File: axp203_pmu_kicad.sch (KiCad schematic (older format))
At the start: 0 parts

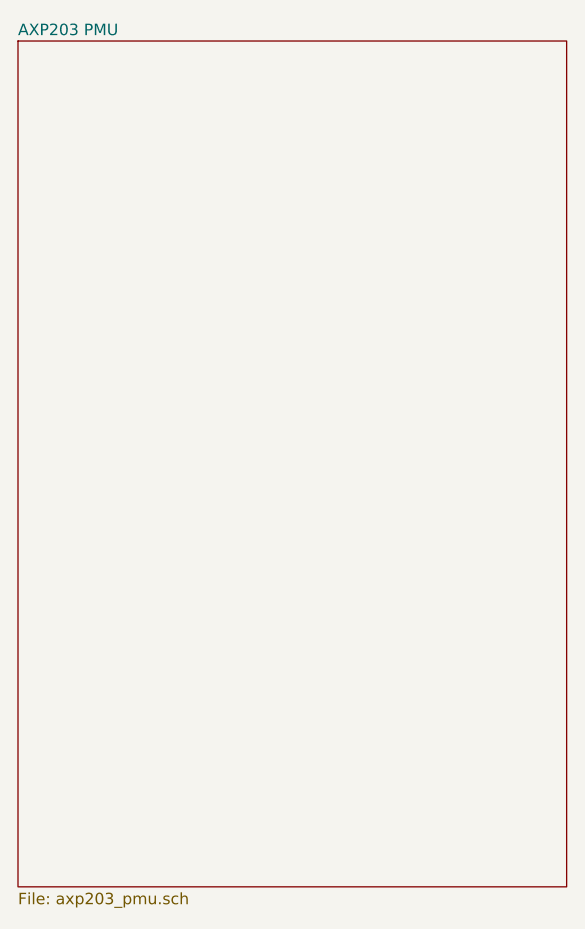
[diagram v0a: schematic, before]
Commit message: Schematic finished, pcb components added in pcb, axp schematic checked
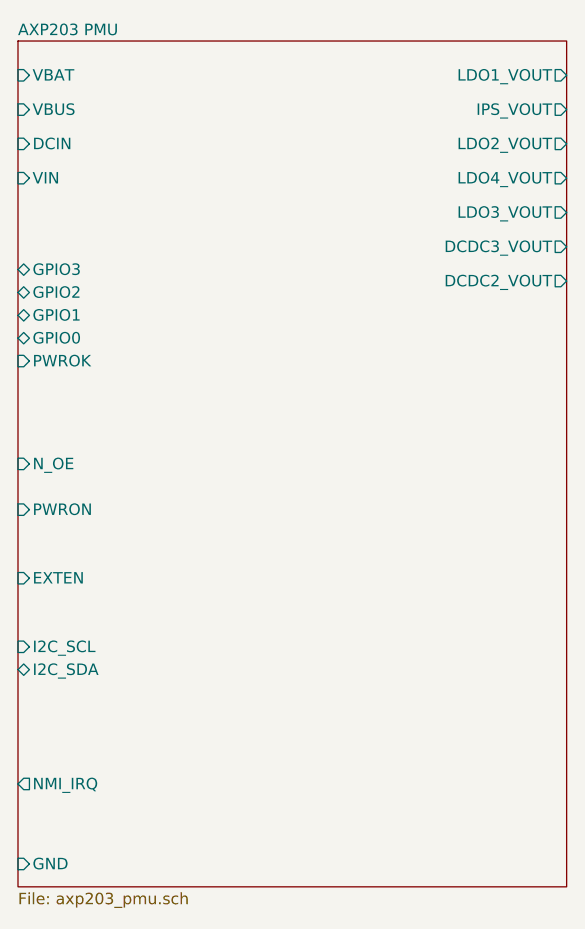
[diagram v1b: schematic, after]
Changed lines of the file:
@@
 F0 "AXP203 PMU" 50
 F1 "axp203_pmu.sch" 50
+F2 "NMI_IRQ" O L 6950 6500 50
+F3 "I2C_SCL" I L 6950 5900 50
+F4 "I2C_SDA" B L 6950 6000 50
+F5 "EXTEN" I L 6950 5600 50
+F6 "GND" I L 6950 6850 50
+F7 "PWRON" I L 6950 5300 50
+F8 "N_OE" I L 6950 5100 50
+F9 "VBAT" I L 6950 3400 50
+F10 "VBUS" I L 6950 3550 50
+F11 "DCIN" I L 6950 3700 50
+F12 "VIN" I L 6950 3850 50
+F13 "LDO1_VOUT" O R 9350 3400 50
+F14 "IPS_VOUT" O R 9350 3550 50
+F15 "LDO2_VOUT" O R 9350 3700 50
+F16 "LDO4_VOUT" O R 9350 3850 50
+F17 "LDO3_VOUT" O R 9350 4000 50
+F18 "DCDC3_VOUT" O R 9350 4150 50
+F19 "DCDC2_VOUT" O R 9350 4300 50
+F20 "GPIO3" B L 6950 4250 50
+F21 "GPIO2" B L 6950 4350 50
+F22 "GPIO1" B L 6950 4450 50
+F23 "GPIO0" B L 6950 4550 50
+F24 "PWROK" I L 6950 4650 50
 $EndSheet
 $EndSCHEMATC
